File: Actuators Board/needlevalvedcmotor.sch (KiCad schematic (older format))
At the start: 33 parts, among them J10 Conn_01x02_Male, J9 Conn_01x02_Male, Q1 MMDT2222A

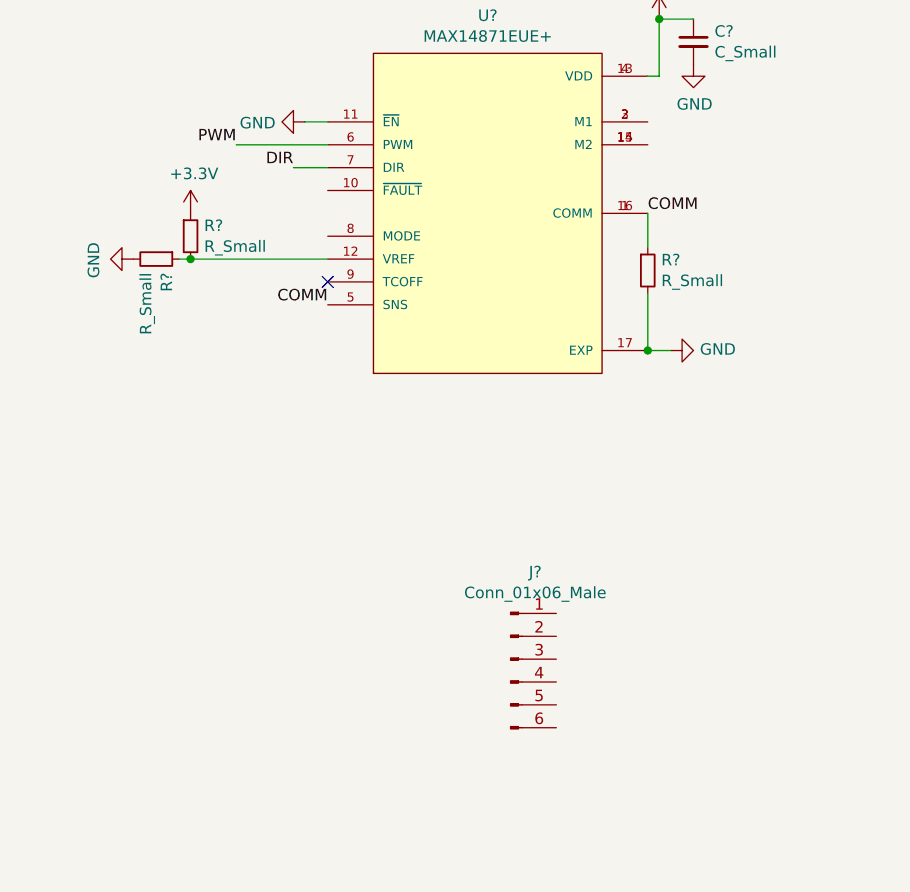
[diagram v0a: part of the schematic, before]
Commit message: Added H-bridge and connector connections
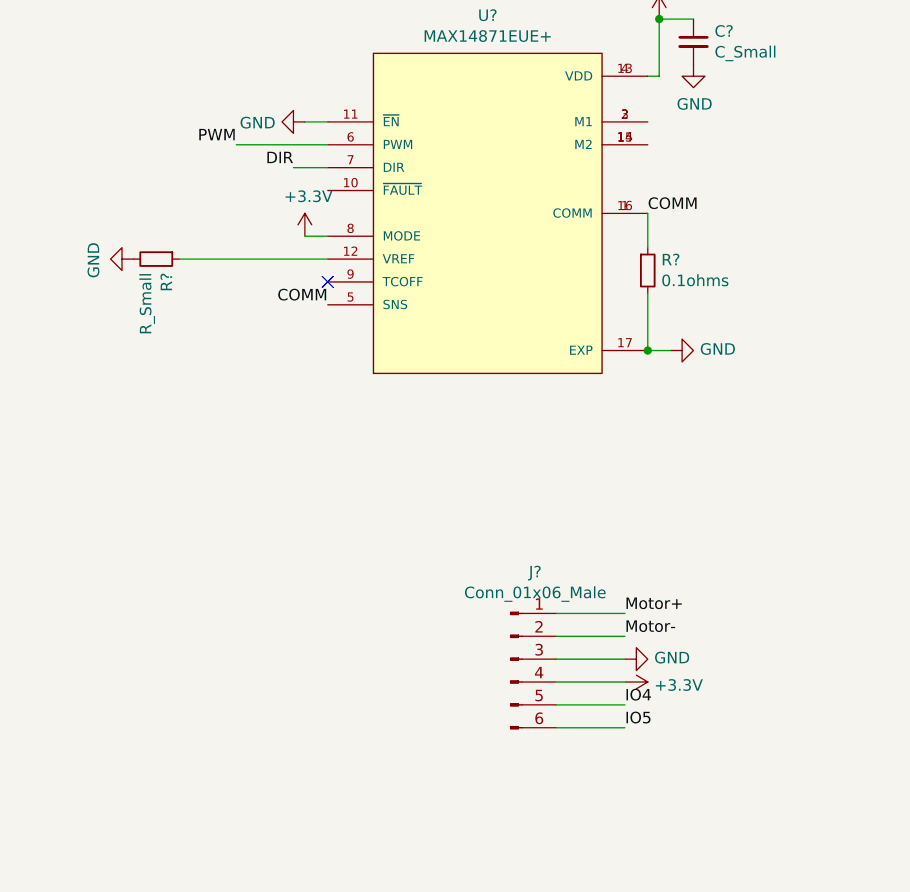
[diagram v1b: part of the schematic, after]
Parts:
- removed R?: R_Small, symbol Device:R_Small
- R?: value R_Small -> 0.1ohms
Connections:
- net +3V3: now also J?.4 (Pin_4), U?.8 (MODE)
- net GND: now also J?.3 (Pin_3)
- net Motor+: now reaches J?.1 (Pin_1)
- net Motor-: now reaches J?.2 (Pin_2)
- net IO4: now reaches J?.5 (Pin_5)
- net IO5: now reaches J?.6 (Pin_6)
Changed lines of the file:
@@
-$Comp
-L Device:R_Small R?
-U 1 1 61950B41
-P 6750 1900
-F 0 "R?" H 6809 1946 50  0000 L CNN
-F 1 "R_Small" H 6809 1855 50  0000 L CNN
-F 2 "" H 6750 1900 50  0001 C CNN
-F 3 "~" H 6750 1900 50  0001 C CNN
-	1    6750 1900
-	1    0    0    -1
-$EndComp
-$Comp
-L power:+3.3V #PWR?
-U 1 1 6195168F
-P 6750 1800
-F 0 "#PWR?" H 6750 1650 50  0001 C CNN
-F 1 "+3.3V" H 6765 1973 50  0000 C CNN
-F 2 "" H 6750 1800 50  0001 C CNN
-F 3 "" H 6750 1800 50  0001 C CNN
-	1    6750 1800
-	1    0    0    -1
-$EndComp
-Wire Wire Line
-	6750 2000 6700 2000
 $Comp
 L Device:R_Small R?
@@
 	0    1    1    0
 $EndComp
-Connection ~ 6750 2000
-Wire Wire Line
-	6750 2000 7350 2000
 $Comp
 L power:+24V #PWR?
@@
 P 8750 2050
 F 0 "R?" H 8809 2096 50  0000 L CNN
-F 1 "R_Small" H 8809 2005 50  0000 L CNN
+F 1 "0.1ohms" H 8809 2005 50  0000 L CNN
 F 2 "" H 8750 2050 50  0001 C CNN
 F 3 "~" H 8750 2050 50  0001 C CNN
@@
 $EndComp
 NoConn ~ 7350 2100
+$Comp
+L power:+3.3V #PWR?
+U 1 1 61990603
+P 7250 1900
+F 0 "#PWR?" H 7250 1750 50  0001 C CNN
+F 1 "+3.3V" H 7265 2073 50  0000 C CNN
+F 2 "" H 7250 1900 50  0001 C CNN
+F 3 "" H 7250 1900 50  0001 C CNN
+	1    7250 1900
+	1    0    0    -1
+$EndComp
+Wire Wire Line
+	7250 1900 7350 1900
+Wire Wire Line
+	6700 2000 7350 2000
+Text Label 8650 3550 0    50   ~ 0
+Motor+
+Wire Wire Line
+	8350 3550 8650 3550
+Text Label 8650 3650 0    50   ~ 0
+Motor-
+Wire Wire Line
+	8350 3650 8650 3650
+Wire Wire Line
+	8350 3750 8650 3750
+Wire Wire Line
+	8350 3850 8650 3850
+Wire Wire Line
+	8350 3950 8650 3950
+Wire Wire Line
+	8350 4050 8650 4050
+$Comp
+L power:+3.3V #PWR?
+U 1 1 619A8F60
+P 8650 3850
+F 0 "#PWR?" H 8650 3700 50  0001 C CNN
+F 1 "+3.3V" V 8665 3978 50  0000 L CNN
+F 2 "" H 8650 3850 50  0001 C CNN
+F 3 "" H 8650 3850 50  0001 C CNN
+	1    8650 3850
+	0    1    1    0
+$EndComp
+$Comp
+L power:GND #PWR?
+U 1 1 619AC4EA
+P 8650 3750
+F 0 "#PWR?" H 8650 3500 50  0001 C CNN
+F 1 "GND" V 8655 3622 50  0000 R CNN
+F 2 "" H 8650 3750 50  0001 C CNN
+F 3 "" H 8650 3750 50  0001 C CNN
+	1    8650 3750
+	0    -1   -1   0
+$EndComp
+Text Label 8650 3950 0    50   ~ 0
+IO4
+Text Label 8650 4050 0    50   ~ 0
+IO5
 $EndSCHEMATC

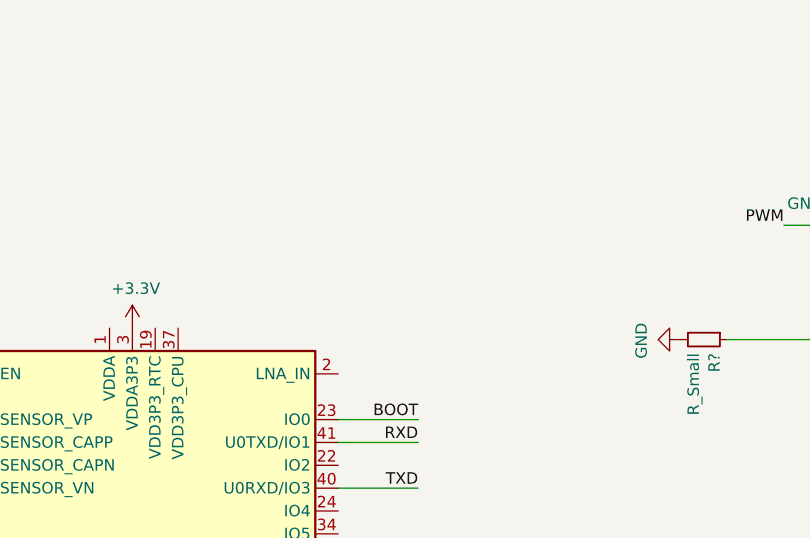
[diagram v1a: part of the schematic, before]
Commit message: Added Rf antenna to all boards
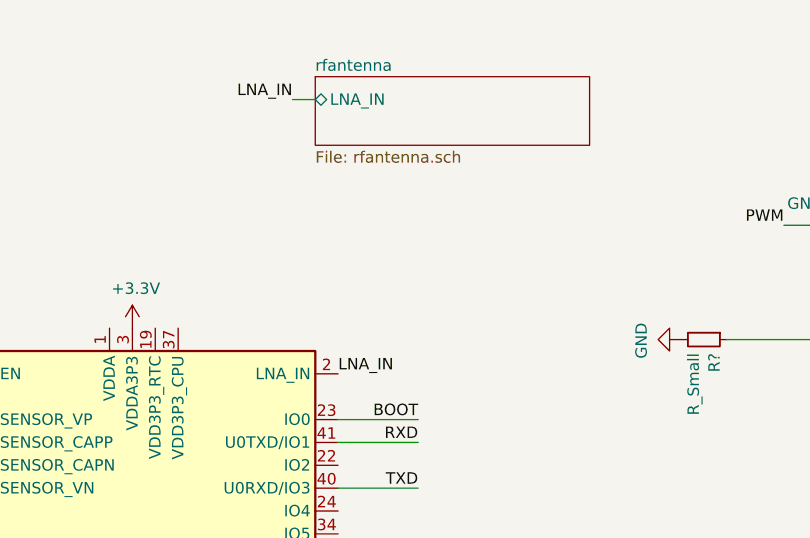
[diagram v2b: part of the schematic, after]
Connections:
- net LNA_IN: now reaches U?.2 (LNA_IN)
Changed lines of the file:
@@
 $Descr A4 11693 8268
 encoding utf-8
-Sheet 1 3
+Sheet 1 4
 Title ""
 Date ""
@@
 Text Label 8650 4050 0    50   ~ 0
 IO5
+$Sheet
+S 4900 850  1200 300
+U 61A238DC
+F0 "rfantenna" 50
+F1 "rfantenna.sch" 50
+F2 "LNA_IN" B L 4900 950 50
+$EndSheet
+Text Label 5000 2150 0    50   ~ 0
+LNA_IN
+Text Label 4800 950  2    50   ~ 0
+LNA_IN
+Wire Wire Line
+	4900 950  4800 950
 $EndSCHEMATC

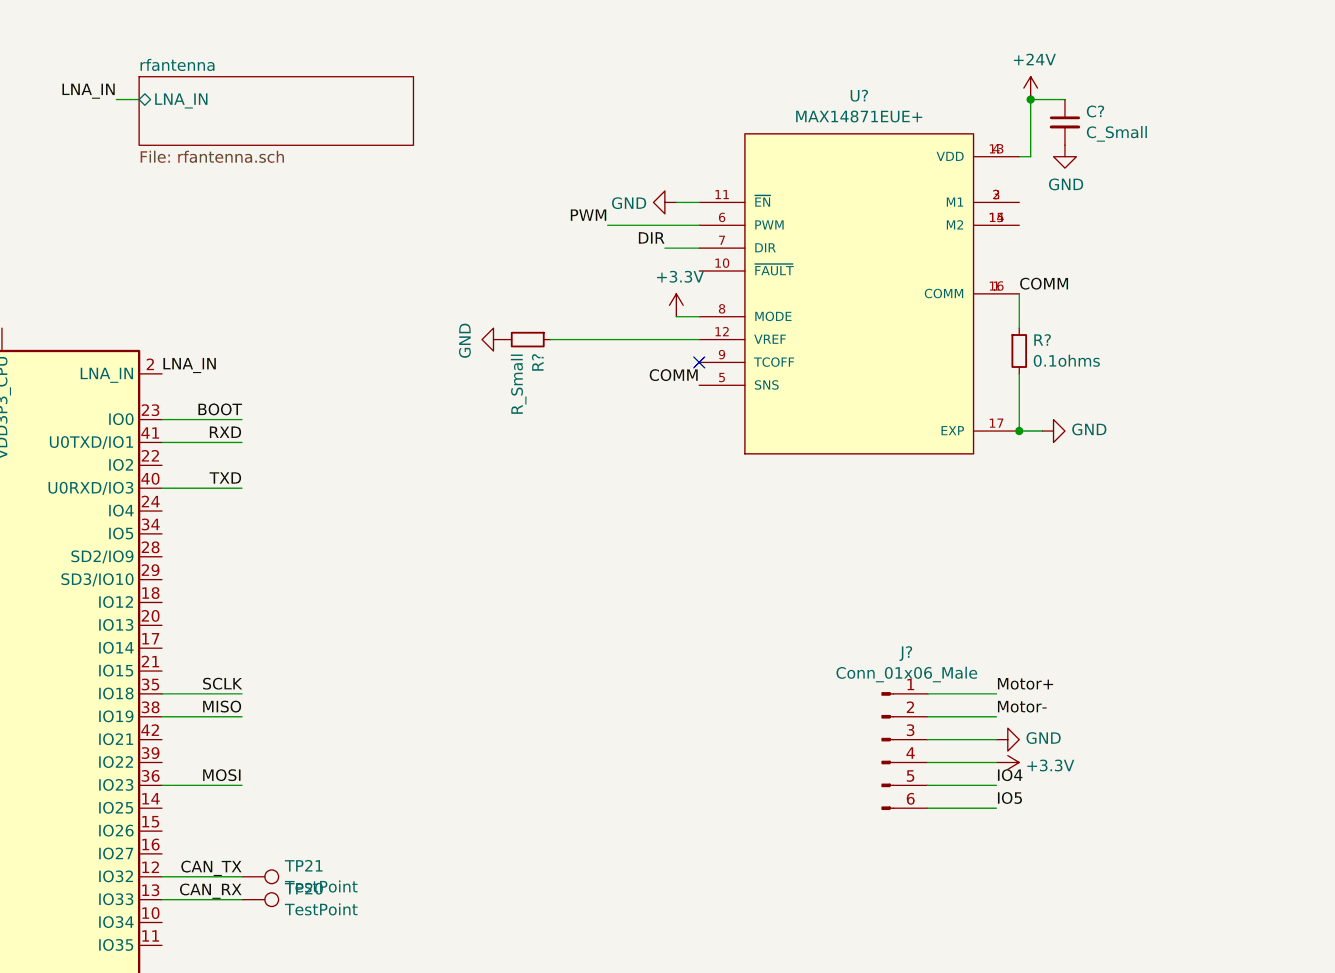
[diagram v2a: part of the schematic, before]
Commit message: Changed capacitance for decoupling cap
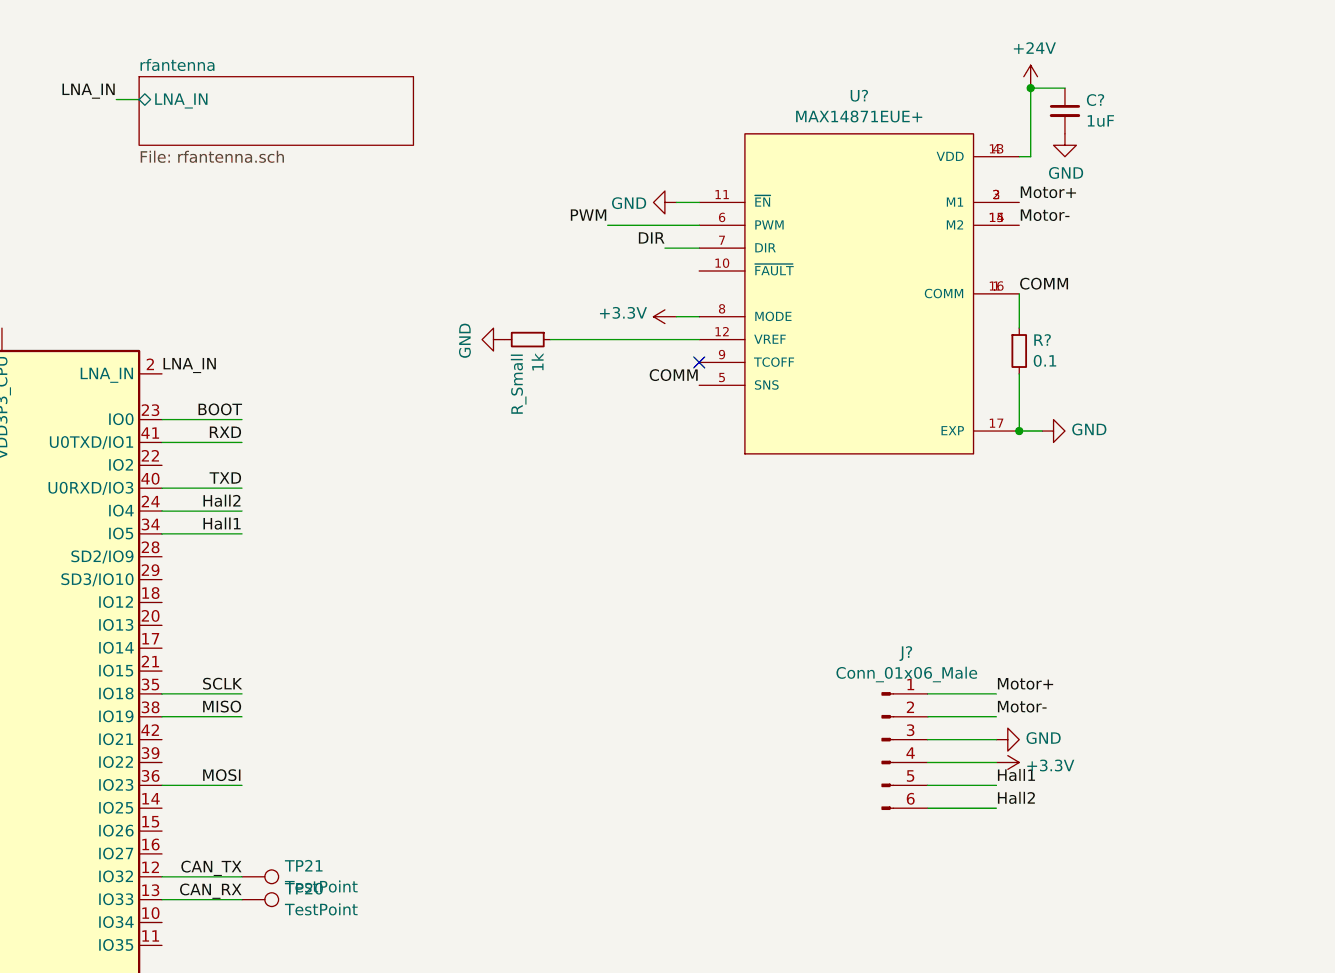
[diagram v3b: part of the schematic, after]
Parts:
- C?: value C_Small -> 1uF
- R?: value 0.1ohms -> 0.1
- gave numbers to parts that had none: 1
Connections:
- net IO4 is gone; now on net Hall1: J?.5 (Pin_5)
- net IO5 is gone; now on net Hall2: J?.6 (Pin_6)
- net Motor+: now also U?.2 (M1), U?.3 (M1)
- net Motor-: now also U?.14 (M2), U?.15 (M2)
- net Hall2: now reaches U?.24 (IO4)
- net Hall1: now reaches U?.34 (IO5)
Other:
- moved on the sheet: C?
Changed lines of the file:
@@
 DIR
 $Comp
-L Device:R_Small R?
+L Device:R_Small 1k
 U 1 1 6195484F
 P 6600 2000
-F 0 "R?" H 6659 2046 50  0000 L CNN
+F 0 "1k" H 6659 2046 50  0000 L CNN
 F 1 "R_Small" H 6659 1955 50  0000 L CNN
 F 2 "" H 6600 2000 50  0001 C CNN
@@
 L power:+24V #PWR?
 U 1 1 619664D0
-P 8800 950
-F 0 "#PWR?" H 8800 800 50  0001 C CNN
-F 1 "+24V" H 8815 1123 50  0000 C CNN
-F 2 "" H 8800 950 50  0001 C CNN
-F 3 "" H 8800 950 50  0001 C CNN
-	1    8800 950
+P 8800 900
+F 0 "#PWR?" H 8800 750 50  0001 C CNN
+F 1 "+24V" H 8815 1073 50  0000 C CNN
+F 2 "" H 8800 900 50  0001 C CNN
+F 3 "" H 8800 900 50  0001 C CNN
+	1    8800 900
 	1    0    0    -1
 $EndComp
 Wire Wire Line
-	8800 950  8950 950
+	8800 900  8950 900
 $Comp
 L Device:C_Small C?
 U 1 1 6196A0BF
-P 8950 1050
-F 0 "C?" H 9042 1096 50  0000 L CNN
-F 1 "C_Small" H 9042 1005 50  0000 L CNN
-F 2 "" H 8950 1050 50  0001 C CNN
-F 3 "~" H 8950 1050 50  0001 C CNN
-	1    8950 1050
+P 8950 1000
+F 0 "C?" H 9042 1046 50  0000 L CNN
+F 1 "1uF" H 9042 955 50  0000 L CNN
+F 2 "" H 8950 1000 50  0001 C CNN
+F 3 "~" H 8950 1000 50  0001 C CNN
+	1    8950 1000
 	1    0    0    -1
 $EndComp
@@
 L power:GND #PWR?
 U 1 1 6196B318
-P 8950 1150
-F 0 "#PWR?" H 8950 900 50  0001 C CNN
-F 1 "GND" H 8955 977 50  0000 C CNN
-F 2 "" H 8950 1150 50  0001 C CNN
-F 3 "" H 8950 1150 50  0001 C CNN
-	1    8950 1150
+P 8950 1100
+F 0 "#PWR?" H 8950 850 50  0001 C CNN
+F 1 "GND" H 8955 927 50  0000 C CNN
+F 2 "" H 8950 1100 50  0001 C CNN
+F 3 "" H 8950 1100 50  0001 C CNN
+	1    8950 1100
 	1    0    0    -1
 $EndComp
 Wire Wire Line
 	8750 1200 8800 1200
-Wire Wire Line
-	8800 1200 8800 950
-Connection ~ 8800 950
 Text Label 7350 2200 2    50   ~ 0
 COMM
@@
 P 8750 2050
 F 0 "R?" H 8809 2096 50  0000 L CNN
-F 1 "0.1ohms" H 8809 2005 50  0000 L CNN
+F 1 "0.1" H 8809 2005 50  0000 L CNN
 F 2 "" H 8750 2050 50  0001 C CNN
 F 3 "~" H 8750 2050 50  0001 C CNN
@@
 $EndComp
 NoConn ~ 7350 2100
-$Comp
-L power:+3.3V #PWR?
-U 1 1 61990603
-P 7250 1900
-F 0 "#PWR?" H 7250 1750 50  0001 C CNN
-F 1 "+3.3V" H 7265 2073 50  0000 C CNN
-F 2 "" H 7250 1900 50  0001 C CNN
-F 3 "" H 7250 1900 50  0001 C CNN
-	1    7250 1900
-	1    0    0    -1
-$EndComp
 Wire Wire Line
 	7250 1900 7350 1900
@@
 	0    -1   -1   0
 $EndComp
-Text Label 8650 3950 0    50   ~ 0
-IO4
-Text Label 8650 4050 0    50   ~ 0
-IO5
 $Sheet
 S 4900 850  1200 300
@@
 Wire Wire Line
 	4900 950  4800 950
+Text Label 8750 1400 0    50   ~ 0
+Motor+
+Wire Wire Line
+	8800 900  8800 1200
+Connection ~ 8800 900
+Text Label 8750 1500 0    50   ~ 0
+Motor-
+Text Label 8650 3950 0    50   ~ 0
+Hall1
+Text Label 8650 4050 0    50   ~ 0
+Hall2
+Text Label 5350 2850 2    50   ~ 0
+Hall1
+Text Label 5350 2750 2    50   ~ 0
+Hall2
+$Comp
+L power:+3.3V #PWR?
+U 1 1 61A368CC
+P 7250 1900
+F 0 "#PWR?" H 7250 1750 50  0001 C CNN
+F 1 "+3.3V" V 7265 2028 50  0000 L CNN
+F 2 "" H 7250 1900 50  0001 C CNN
+F 3 "" H 7250 1900 50  0001 C CNN
+	1    7250 1900
+	0    -1   -1   0
+$EndComp
+Wire Wire Line
+	5000 2750 5350 2750
+Wire Wire Line
+	5000 2850 5350 2850
 $EndSCHEMATC

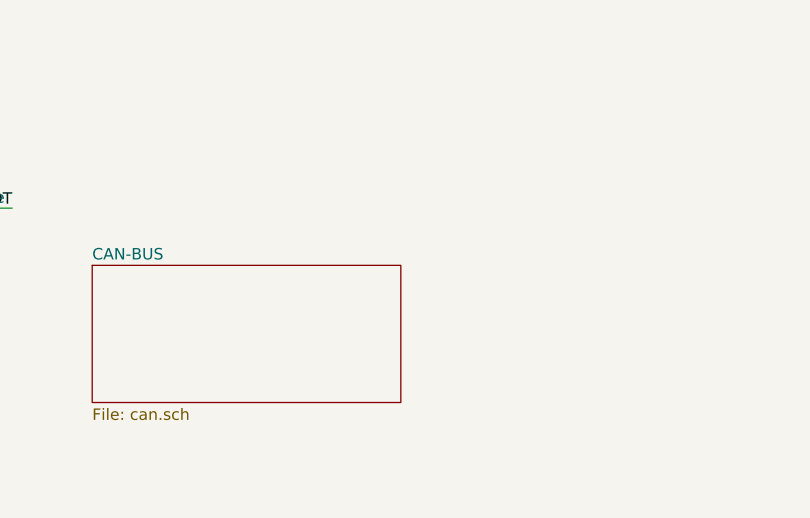
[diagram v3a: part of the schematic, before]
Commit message: Place Hierarchical Pins from CAN sheet to each board.
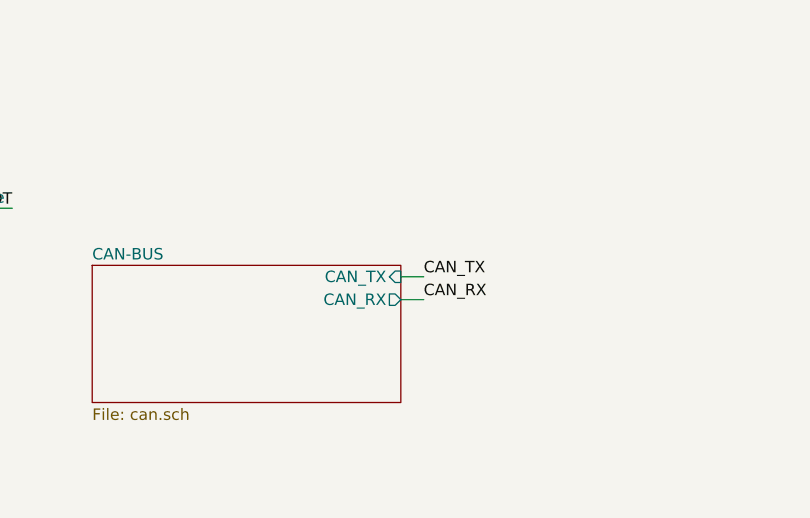
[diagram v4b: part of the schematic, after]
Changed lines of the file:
@@
 F0 "CAN-BUS" 50
 F1 "can.sch" 50
+F2 "CAN_TX" I R 4600 6800 50
+F3 "CAN_RX" O R 4600 6900 50
 $EndSheet
 $Comp
@@
 Wire Wire Line
 	5000 2850 5350 2850
+Wire Wire Line
+	4600 6800 4700 6800
+Wire Wire Line
+	4600 6900 4700 6900
+Text Label 4700 6800 0    50   ~ 0
+CAN_TX
+Text Label 4700 6900 0    50   ~ 0
+CAN_RX
 $EndSCHEMATC
